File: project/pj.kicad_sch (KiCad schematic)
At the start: 15 parts, among them J1 RPi_GPIO, J10 Pico PWR enable, J2 2B+, J3 zero, J4 3A+, J5 3B+, J6 4, J7 Conn_01x02, J8 Conn_01x02, J9 External PWR, SW1 SW_Push, SW2 SW_Push

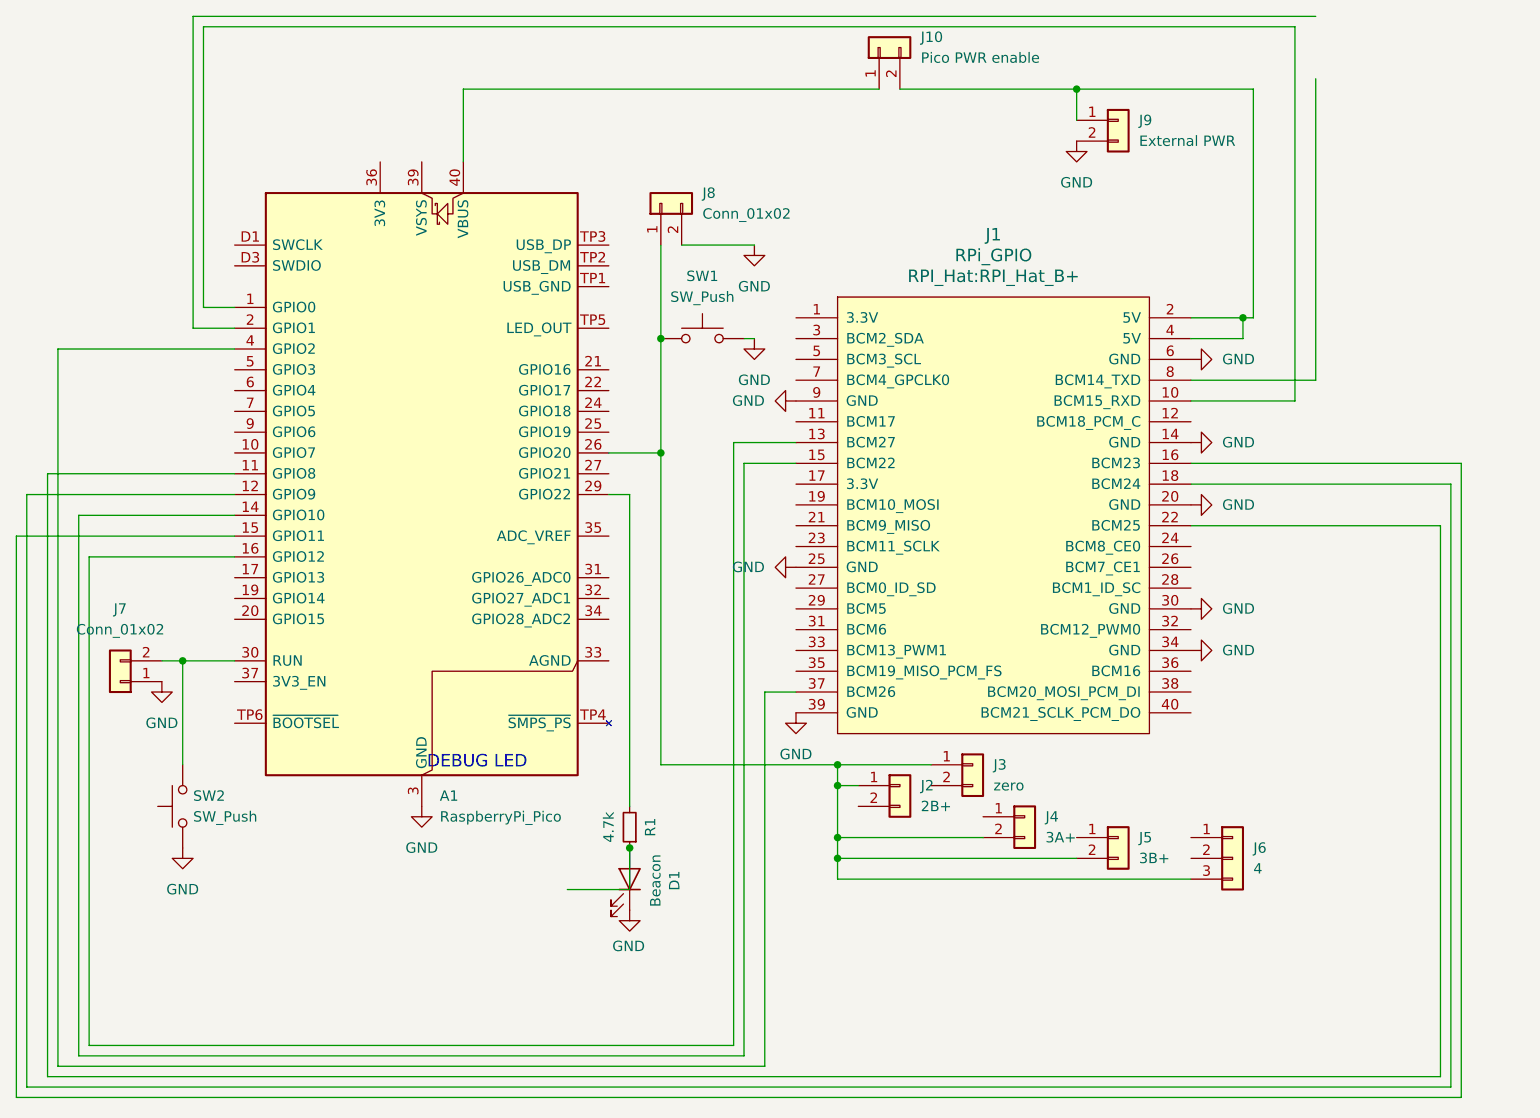
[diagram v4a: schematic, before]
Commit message: add gpio bus, lables and KiCad logo
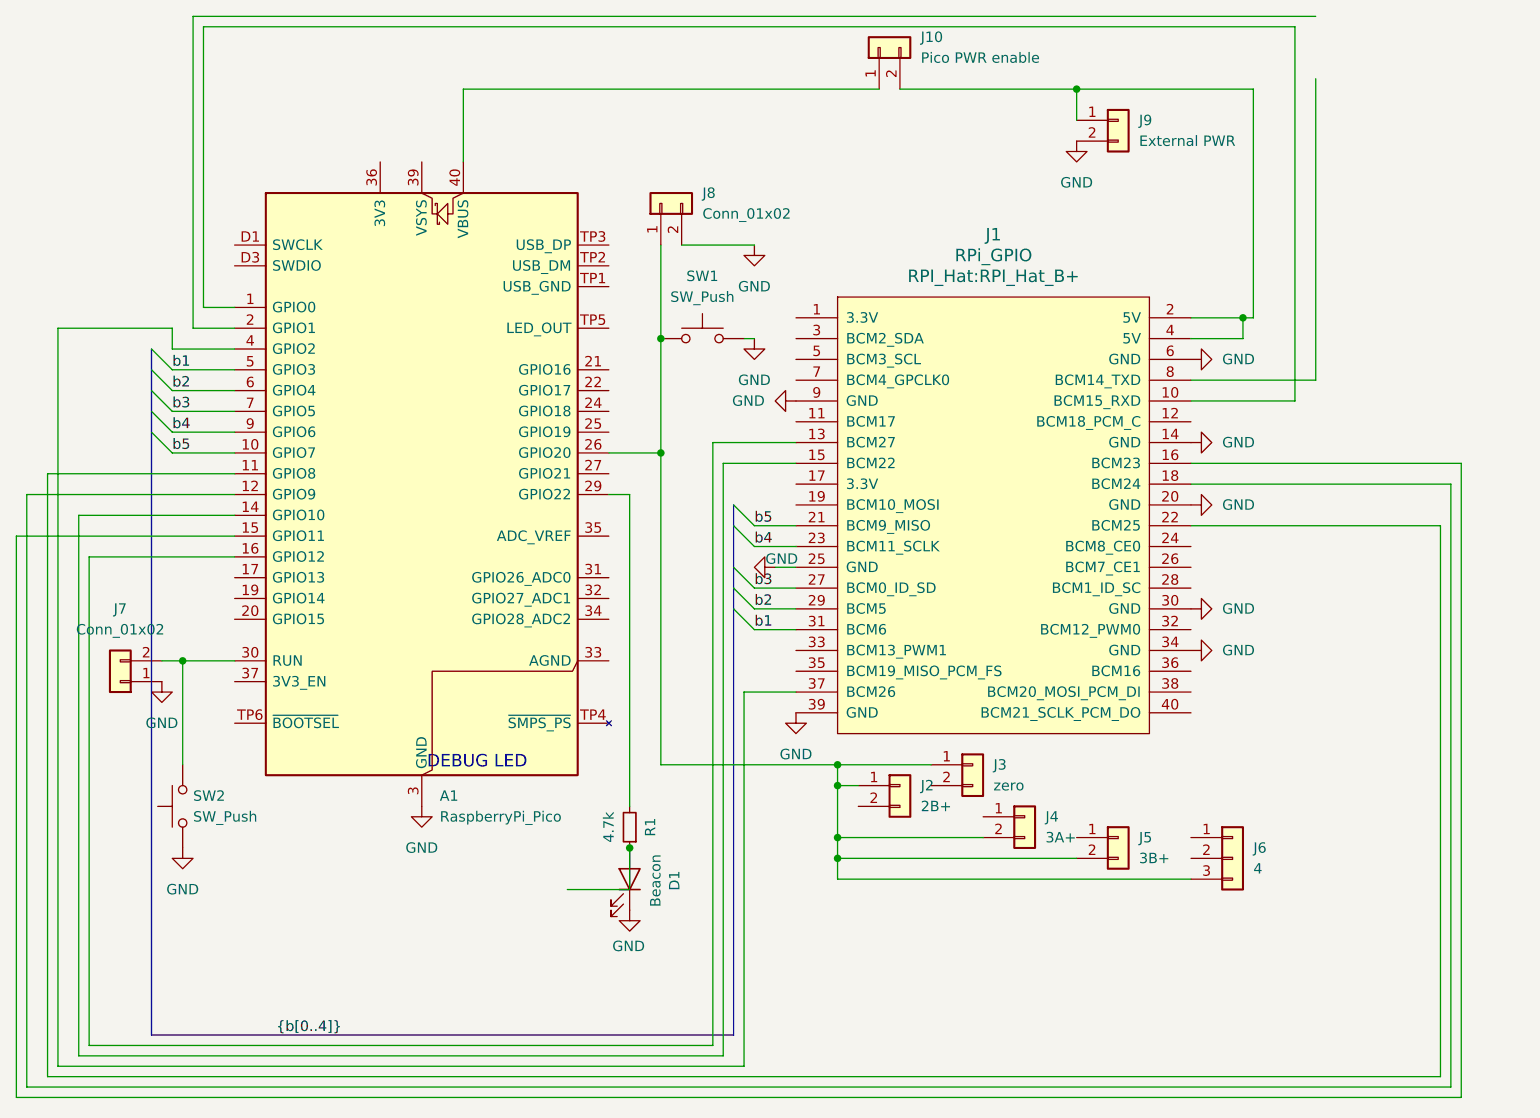
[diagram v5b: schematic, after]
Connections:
- net b5: now reaches A1.10 (GPIO7)
- net b5: now also J1.21 (BCM9_MISO)
- net b1: now reaches A1.5 (GPIO3)
- net b1: now also J1.31 (BCM6)
- net b2: now reaches A1.6 (GPIO4)
- net b2: now also J1.29 (BCM5)
- net b3: now reaches A1.7 (GPIO5)
- net b3: now also J1.27 (BCM0_ID_SD)
- net b4: now reaches A1.9 (GPIO6)
- net b4: now also J1.23 (BCM11_SCLK)

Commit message: group jtag io
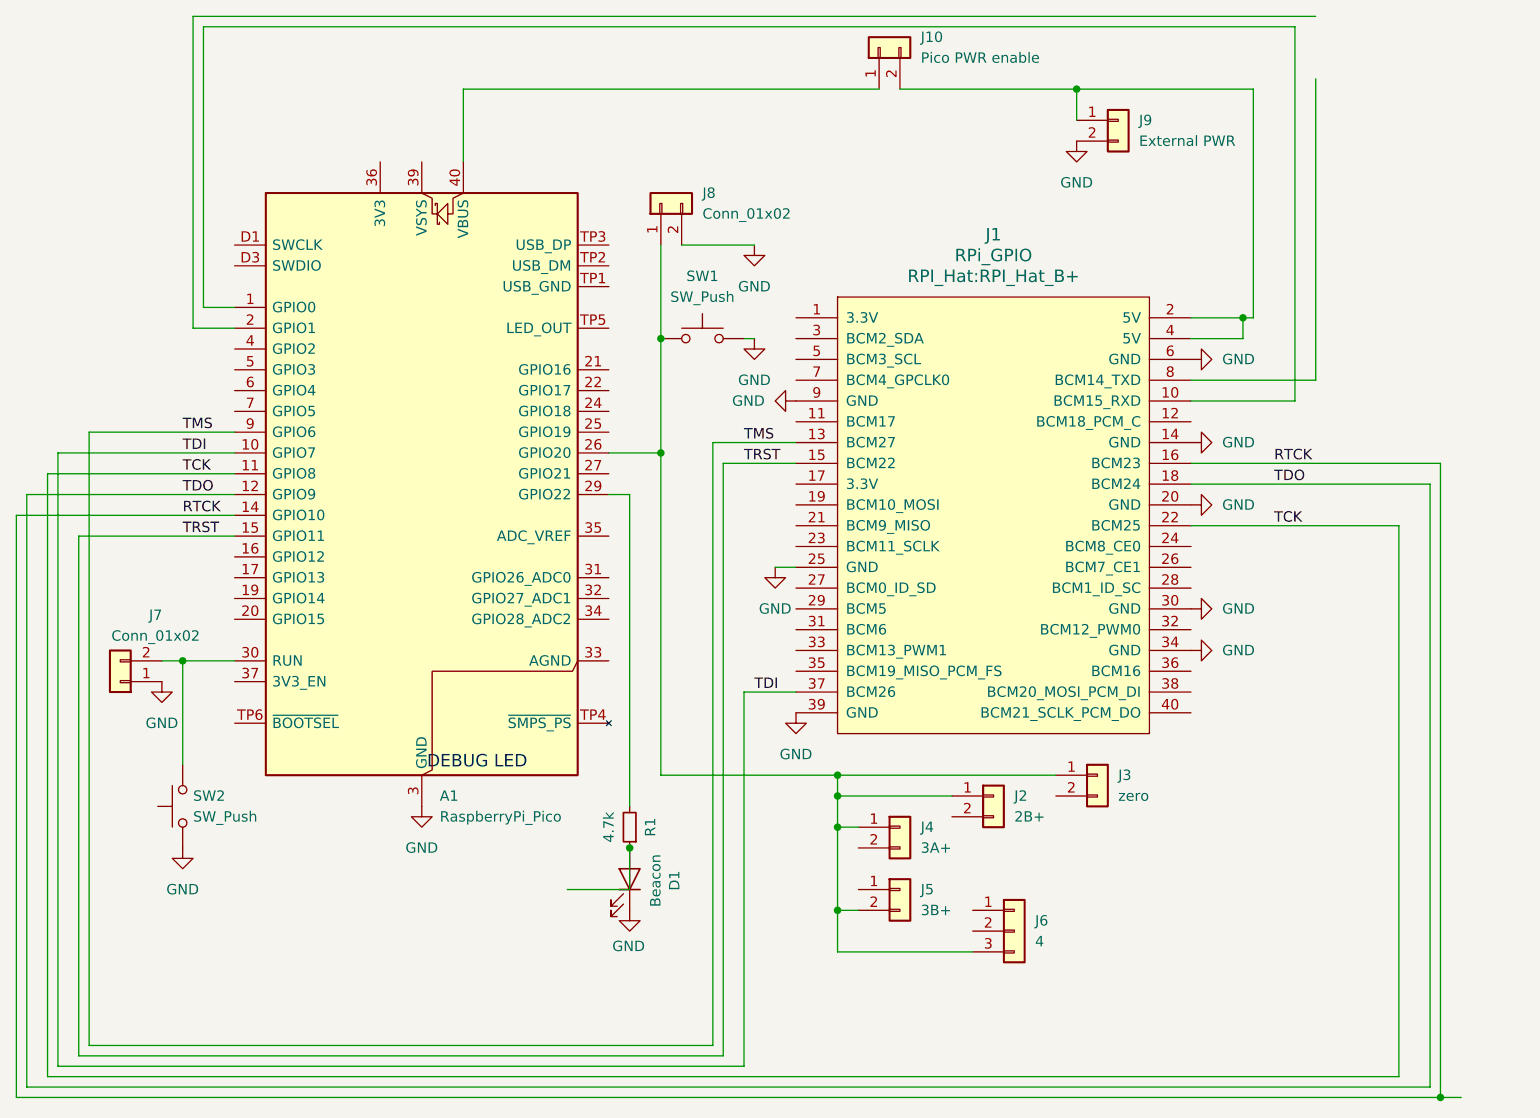
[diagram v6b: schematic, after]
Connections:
- net at A1.26 (GPIO20), J2.1 (Pin_1), J3.1 (Pin_1)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: now also J4.1 (Pin_1); no longer J4.2 (Pin_2)
- net TCK: now reaches A1.11 (GPIO8), J1.22 (BCM25)
- net TDO: now reaches A1.12 (GPIO9), J1.18 (BCM24)
- net RTCK: now reaches A1.14 (GPIO10)
- net RTCK: now also J1.16 (BCM23); no longer J1.15 (BCM22)
- net TRST: now reaches A1.15 (GPIO11)
- net TRST: now also J1.15 (BCM22); no longer J1.16 (BCM23)
- net at A1.16 (GPIO12): no longer J1.13 (BCM27)
- net at A1.4 (GPIO2): no longer J1.37 (BCM26)
- net b1: no longer names the net of A1.5 (GPIO3)
- net b1: no longer J1.31 (BCM6)
- net b2: no longer names the net of A1.6 (GPIO4)
- net b2: no longer J1.29 (BCM5)
- net b3: no longer names the net of A1.7 (GPIO5)
- net b3: no longer J1.27 (BCM0_ID_SD)
- net b4: no longer names the net of J1.23 (BCM11_SCLK)
- net b4: no longer A1.9 (GPIO6)
- net b5: no longer names the net of J1.21 (BCM9_MISO)
- net b5: no longer A1.10 (GPIO7)
- new net TDI: A1.10 (GPIO7), J1.37 (BCM26)
- new net TMS: A1.9 (GPIO6), J1.13 (BCM27)
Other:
- moved on the sheet: J2, J3, J4, J5, J6

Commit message: move the pi reset jumper/button schematic
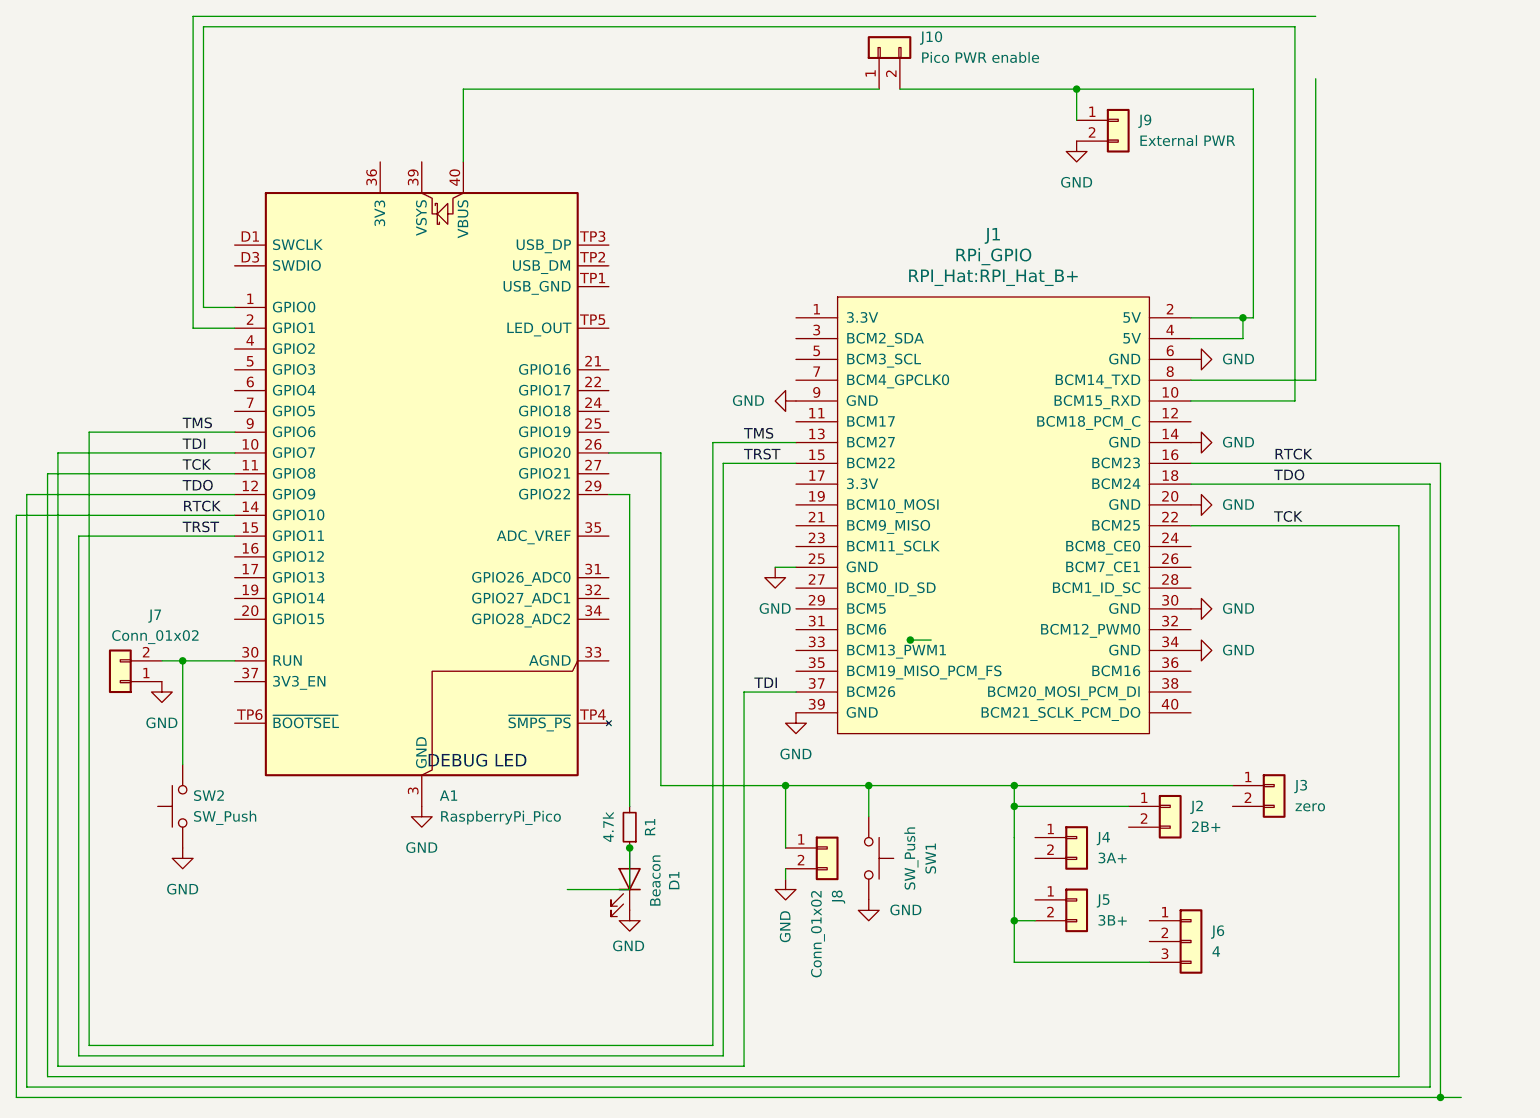
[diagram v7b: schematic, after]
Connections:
- net at A1.26 (GPIO20), J2.1 (Pin_1), J3.1 (Pin_1)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: no longer J4.1 (Pin_1)
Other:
- moved on the sheet: J2, J3, J4, J5, J6, J8, SW1

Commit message: hook some gpios for kicks
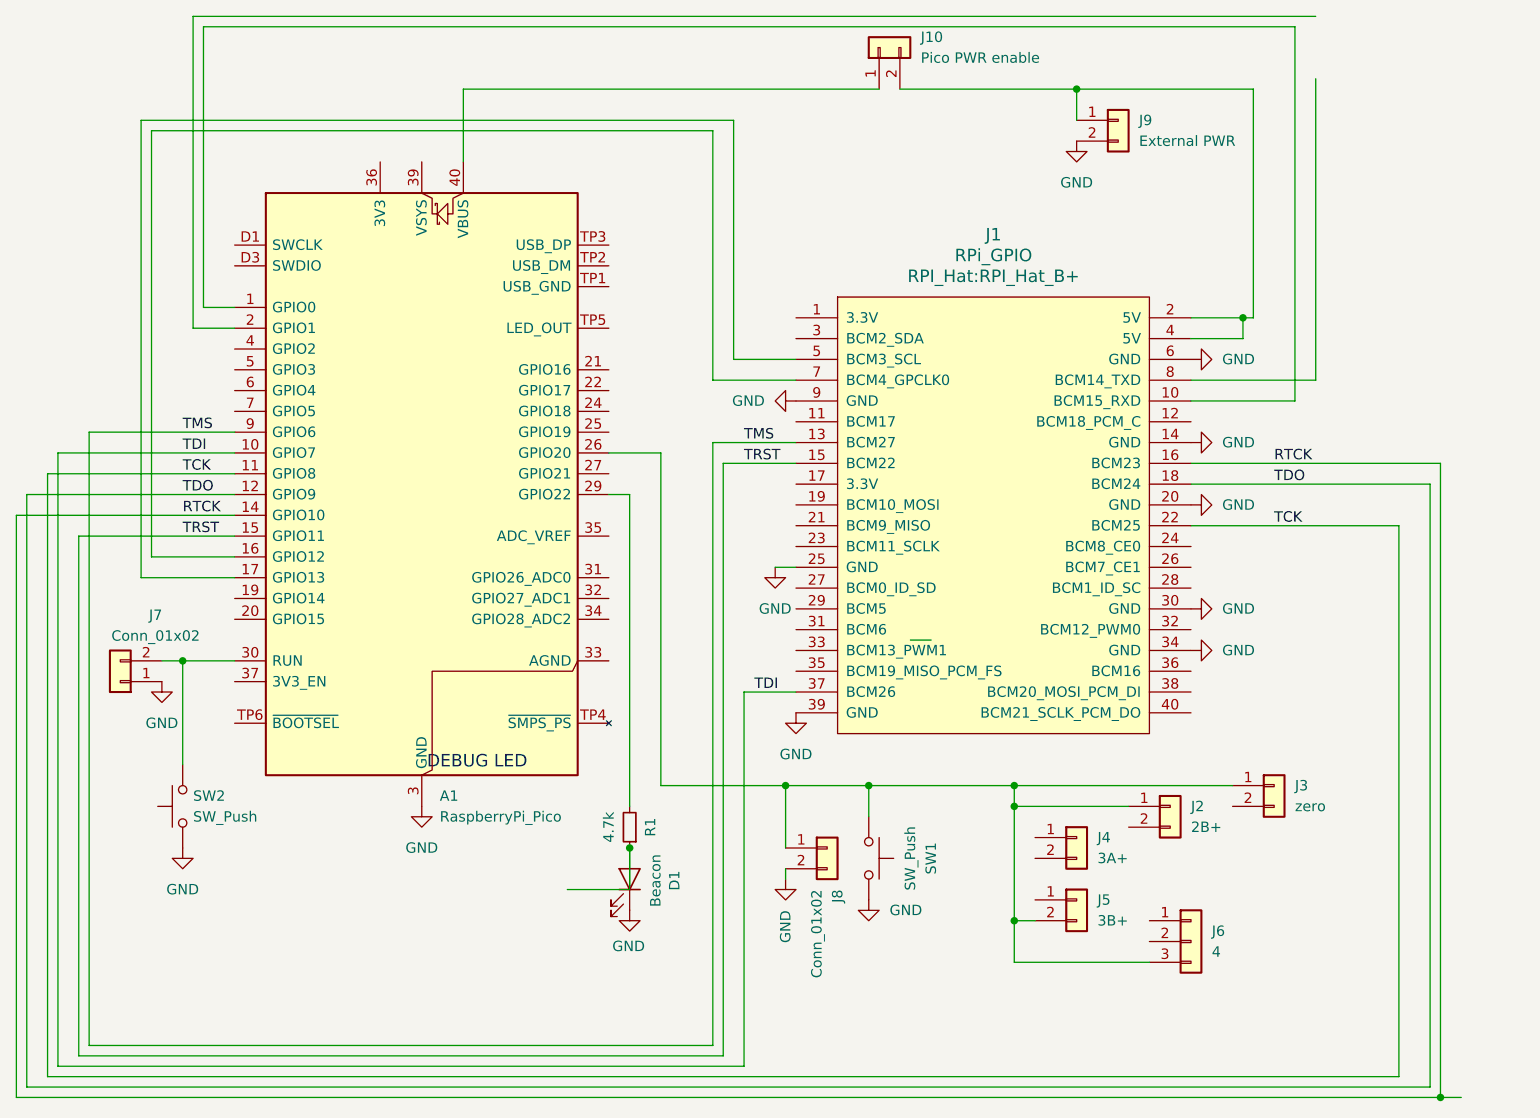
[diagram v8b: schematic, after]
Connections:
- net at A1.16 (GPIO12): now also J1.7 (BCM4_GPCLK0)
- net at A1.17 (GPIO13): now also J1.5 (BCM3_SCL)
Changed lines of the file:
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@@
 		(color 0 0 0 0)
 	)
-	(junction
-		(at 146.05 95.25)
-		(diameter 0)
-		(color 0 0 0 0)
-	)
 	(wire
 		(pts
@@
 	(wire
 		(pts
+			(xy 53.34 33.02) (xy 121.92 33.02)
+		)
+		(stroke
+			(width 0)
+			(type default)
+		)
+	)
+	(wire
+		(pts
 			(xy 205.74 148.59) (xy 40.64 148.59)
 		)
@@
 	(wire
 		(pts
+			(xy 53.34 85.09) (xy 53.34 33.02)
+		)
+		(stroke
+			(width 0)
+			(type default)
+		)
+	)
+	(wire
+		(pts
 			(xy 210.82 73.66) (xy 210.82 151.13)
 		)
@@
 	(wire
 		(pts
+			(xy 121.92 33.02) (xy 121.92 63.5)
+		)
+		(stroke
+			(width 0)
+			(type default)
+		)
+	)
+	(wire
+		(pts
+			(xy 52.07 87.63) (xy 63.5 87.63)
+		)
+		(stroke
+			(width 0)
+			(type default)
+		)
+	)
+	(wire
+		(pts
 			(xy 45.72 69.85) (xy 63.5 69.85)
 		)
@@
 	(wire
 		(pts
+			(xy 124.46 31.75) (xy 52.07 31.75)
+		)
+		(stroke
+			(width 0)
+			(type default)
+		)
+	)
+	(wire
+		(pts
 			(xy 144.78 27.94) (xy 166.37 27.94)
 		)
@@
 	(wire
 		(pts
+			(xy 63.5 85.09) (xy 53.34 85.09)
+		)
+		(stroke
+			(width 0)
+			(type default)
+		)
+	)
+	(wire
+		(pts
 			(xy 166.37 27.94) (xy 187.96 27.94)
 		)
@@
 	(wire
 		(pts
-			(xy 158.75 115.57) (xy 158.75 119.38)
-		)
-		(stroke
-			(width 0)
-			(type default)
-		)
-	)
-	(wire
-		(pts
 			(xy 40.64 74.93) (xy 63.5 74.93)
 		)
@@
 	(wire
 		(pts
+			(xy 132.08 60.96) (xy 124.46 60.96)
+		)
+		(stroke
+			(width 0)
+			(type default)
+		)
+	)
+	(wire
+		(pts
 			(xy 63.5 72.39) (xy 41.91 72.39)
 		)
@@
 	(wire
 		(pts
+			(xy 124.46 60.96) (xy 124.46 31.75)
+		)
+		(stroke
+			(width 0)
+			(type default)
+		)
+	)
+	(wire
+		(pts
 			(xy 187.96 27.94) (xy 187.96 55.88)
 		)
@@
 	(wire
 		(pts
-			(xy 158.75 119.38) (xy 158.75 129.54)
+			(xy 158.75 115.57) (xy 158.75 129.54)
 		)
 		(stroke
@@
 	(wire
 		(pts
+			(xy 52.07 31.75) (xy 52.07 87.63)
+		)
+		(stroke
+			(width 0)
+			(type default)
+		)
+	)
+	(wire
+		(pts
 			(xy 158.75 129.54) (xy 158.75 134.62)
 		)
@@
 		)
 		(stroke
+			(width 0)
+			(type default)
+		)
+	)
+	(wire
+		(pts
+			(xy 121.92 63.5) (xy 132.08 63.5)
+		)
+		(stroke
